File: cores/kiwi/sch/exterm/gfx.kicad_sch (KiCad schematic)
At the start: 11 parts

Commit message: issue#46
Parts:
- added unit 1 of C6
- added unit 4 of C6
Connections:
- net ~{VBLK} is gone; now on net VBLK: B1.12
- net VBLK: no longer B1.13, C17.58 (~{VBLK})
- net H4B renamed H4_BUF
- net MAB_~{CE}: no longer names the net of E11.19 (~{CE})
- net MAB_~{CE}: now also C6.11
- net MBB_~{CE}: no longer names the net of E12.19 (~{CE})
- net MBB_~{CE}: now also C6.3
- net ~{MAIN_WR} renamed ~{OBJCODELO}
- net ~{WR}: no longer names the net of B6.3
- net ~{WR}: now also C6.12
- new net: B1.13, C17.58 (~{VBLK})
- new net GFX_~{CE}: C6.1
- new net H3_BUF: C6.13, C6.2
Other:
- sheet gfx_ram ports: added H3_BUF; removed H3B
- note removed: "ENABLE"
- moved on the sheet: B1D, B1F, B6A, C6B

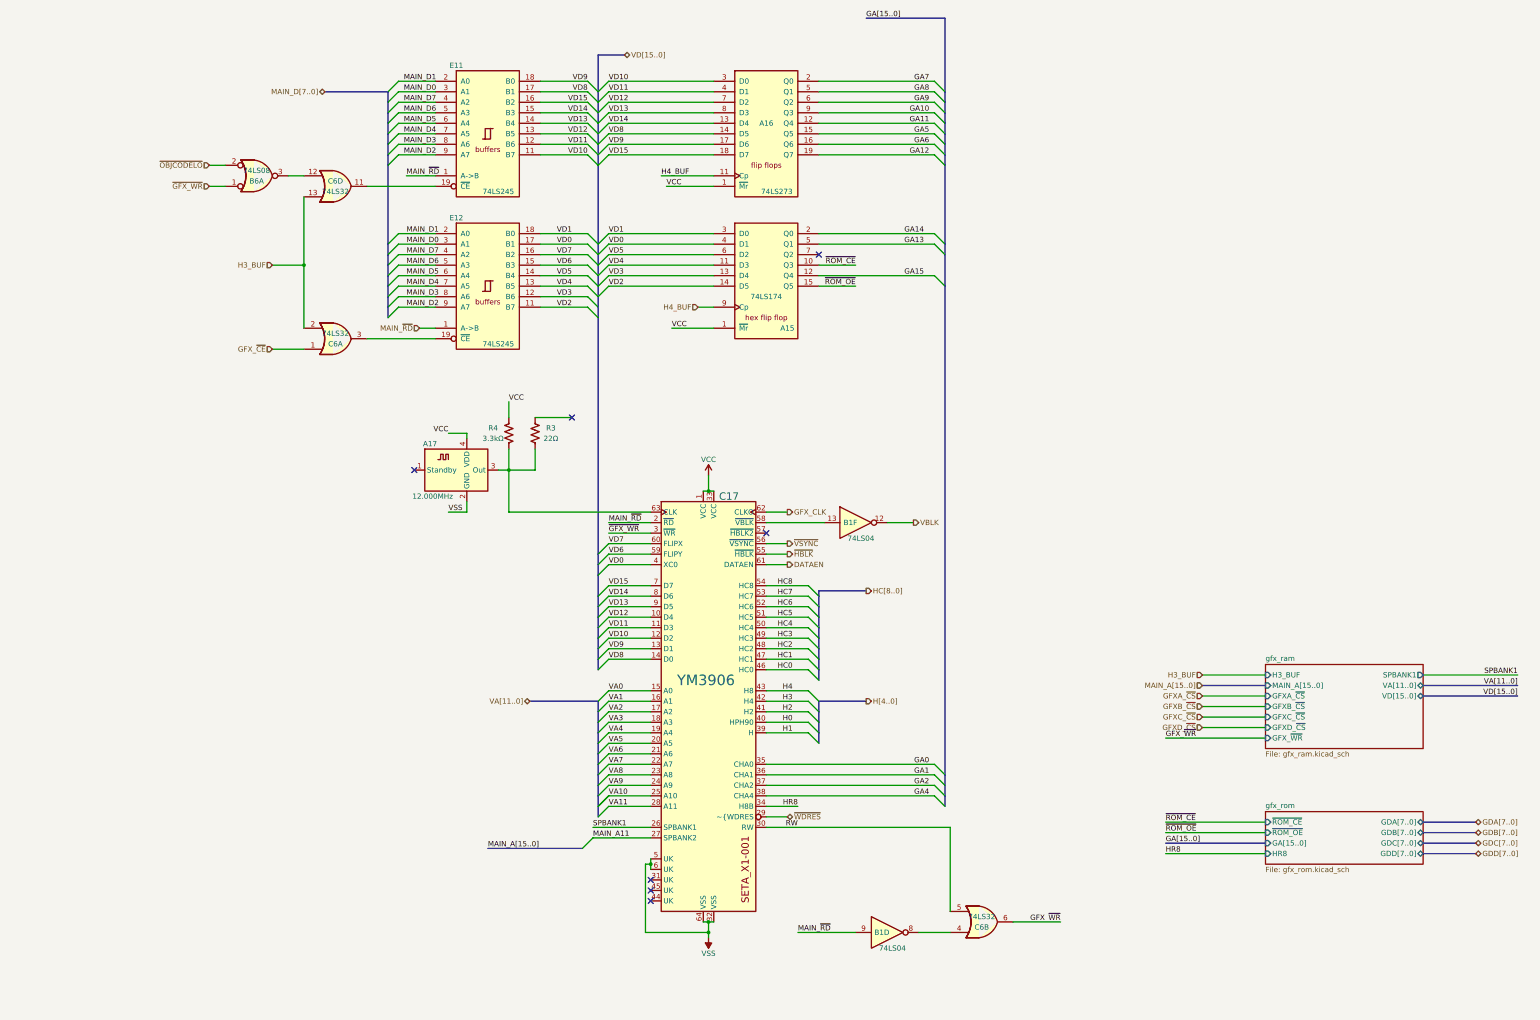
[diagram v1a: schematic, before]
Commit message: sheet_size_update
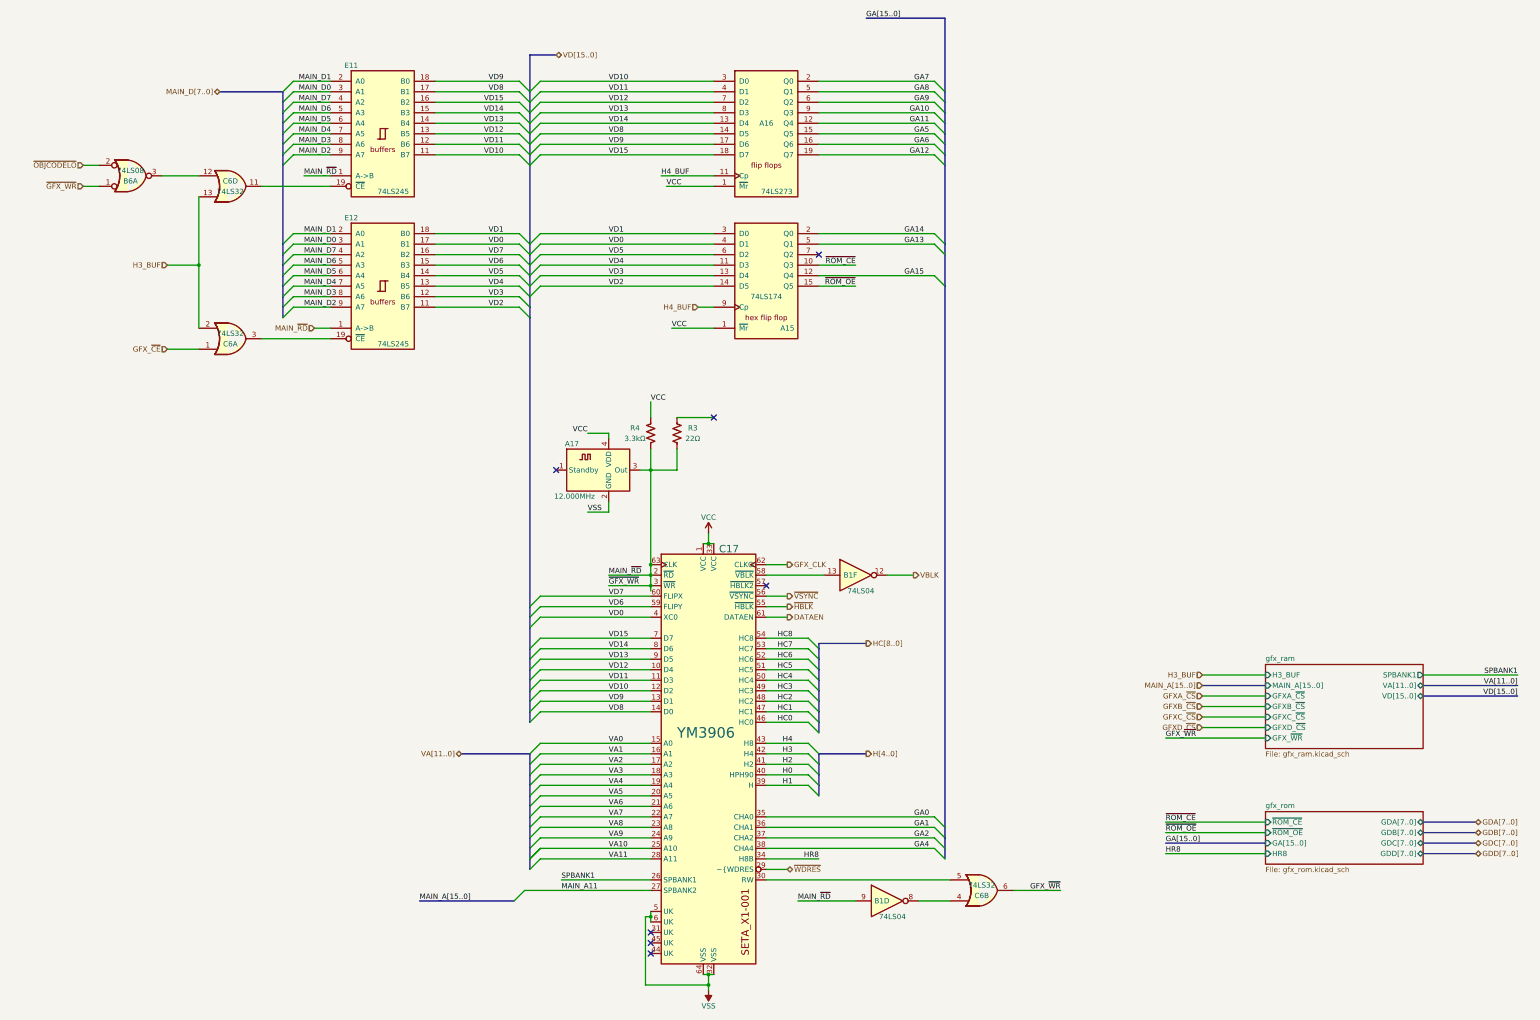
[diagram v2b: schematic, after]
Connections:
- net ~{GFX_WR} is gone; now on net MAIN_~{RD}: B6.1, C17.3 (~{WR})
- net MAIN_~{RD}: now also A17.3 (Out), C17.63 (CLK), R3.2, R4.2
- net RW: no longer names the net of C17.30 (RW), C6.5
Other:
- moved on the sheet: A17, B1D, B1F, B6A, C17, C6A, C6B, C6D, E11, E12, R3, R4

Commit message: cable_correction
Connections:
- net MAIN_~{RD}: no longer A17.3 (Out), B6.1, C17.3 (~{WR}), C17.63 (CLK), R3.2, R4.2
- new net: A17.3 (Out), C17.63 (CLK), R3.2, R4.2
- new net ~{GFX_WR}: B6.1, C17.3 (~{WR})
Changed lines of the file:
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@@
     (comment 1 "E.Triana")
   )
-  (junction (at 181.61 173.99) (diameter 0) (color 0 0 0 0)
-  )
   (junction (at 195.58 267.97) (diameter 0) (color 0 0 0 0)
   )
@@
   )
   (junction (at 181.61 254) (diameter 0) (color 0 0 0 0)
-  )
-  (junction (at 181.61 171.45) (diameter 0) (color 0 0 0 0)
-  )
-  (junction (at 181.61 168.91) (diameter 0) (color 0 0 0 0)
   )
   (no_connect (at 158.75 146.05))
@@
     (stroke (width 0) (type default) (color 0 0 0 0))
   )
-  (wire (pts (xy 181.61 173.99) (xy 181.61 175.26))
-    (stroke (width 0) (type default) (color 0 0 0 0))
-  )
   (bus (pts (xy 252.73 69.85) (xy 252.73 67.31))
     (stroke (width 0) (type default) (color 0 0 0 0))
@@
     (stroke (width 0) (type default) (color 0 0 0 0))
   )
-  (wire (pts (xy 181.61 173.99) (xy 181.61 171.45))
-    (stroke (width 0) (type default) (color 0 0 0 0))
-  )
   (bus (pts (xy 152.4 99.06) (xy 152.4 101.6))
     (stroke (width 0) (type default) (color 0 0 0 0))
@@
     (stroke (width 0) (type default) (color 0 0 0 0))
   )
-  (wire (pts (xy 181.61 171.45) (xy 181.61 168.91))
-    (stroke (width 0) (type default) (color 0 0 0 0))
-  )
